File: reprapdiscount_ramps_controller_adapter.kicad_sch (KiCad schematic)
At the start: 5 parts

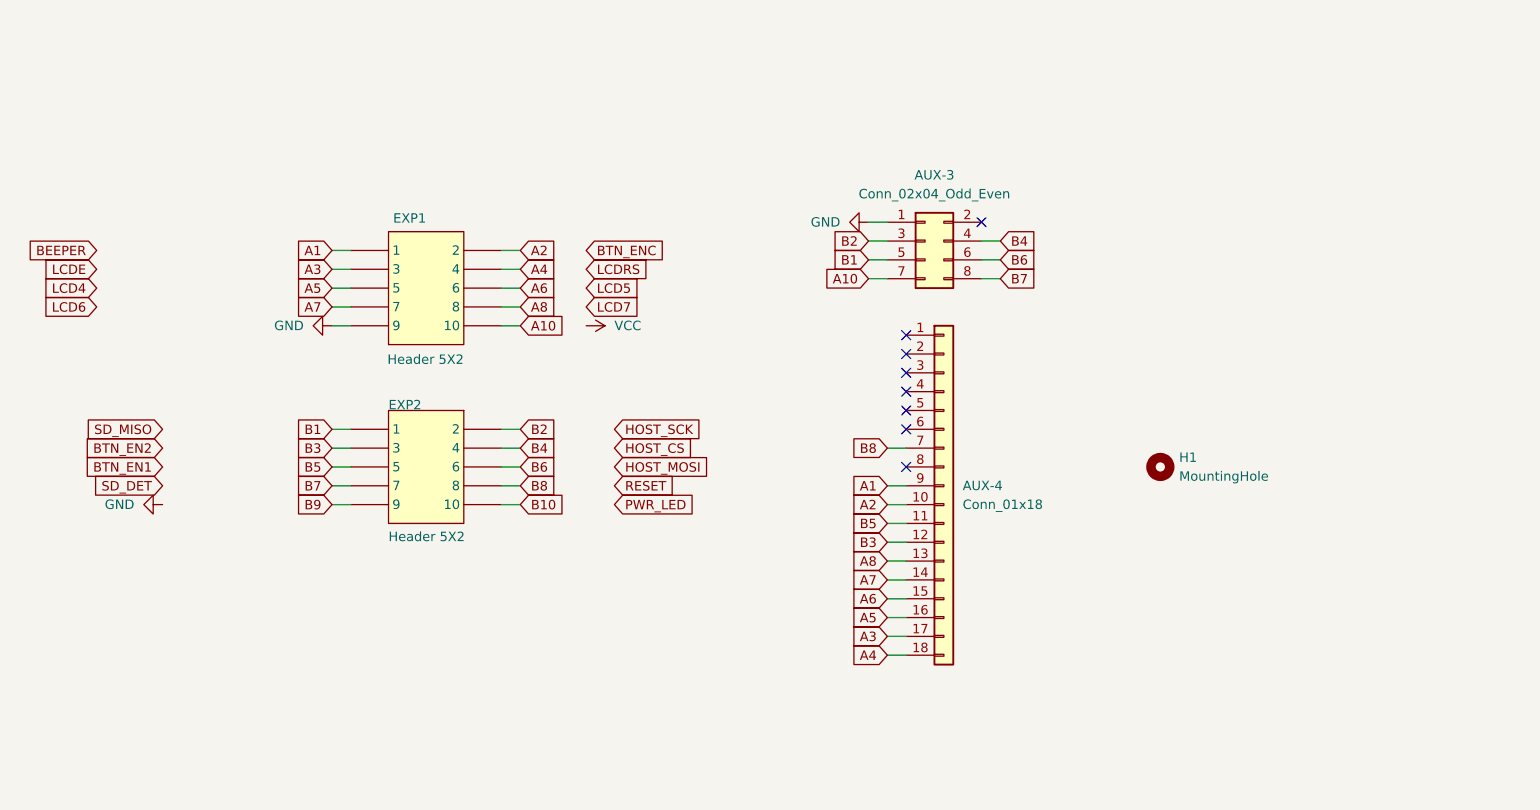
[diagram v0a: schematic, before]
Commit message: adapter: clean up schematic
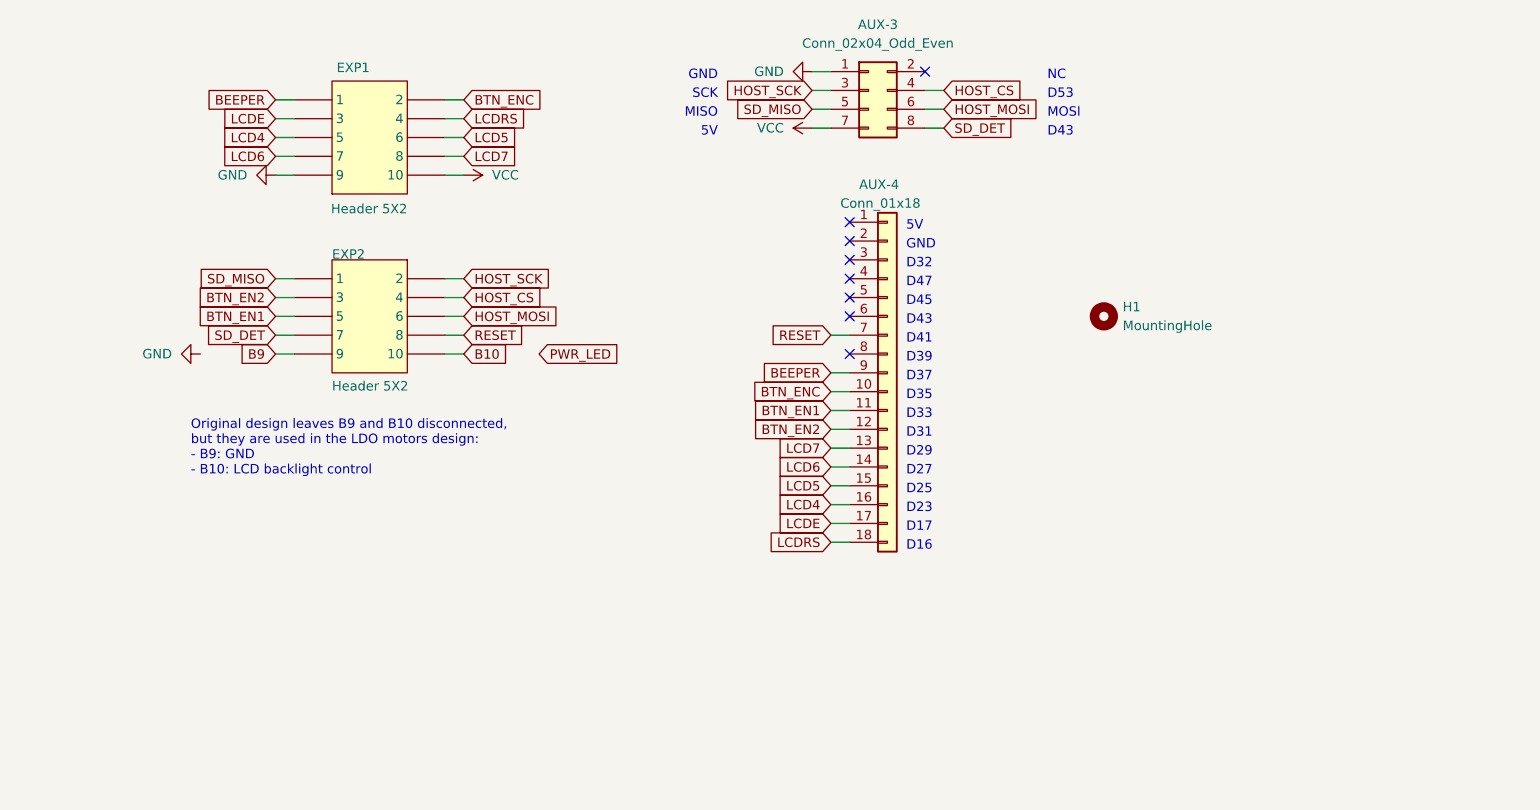
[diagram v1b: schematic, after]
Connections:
- net A1 is gone; now on net BEEPER: AUX-4.9 (Pin_9), EXP1.1
- net A10 is gone; now on net VCC: AUX-3.7 (Pin_7), EXP1.10
- net A2 is gone; now on net BTN_ENC: AUX-4.10 (Pin_10), EXP1.2
- net A3 is gone; now on net LCDE: AUX-4.17 (Pin_17), EXP1.3
- net A4 is gone; now on net LCDRS: AUX-4.18 (Pin_18), EXP1.4
- net A5 is gone; now on net LCD4: AUX-4.16 (Pin_16), EXP1.5
- net A6 is gone; now on net LCD5: AUX-4.15 (Pin_15), EXP1.6
- net A7 is gone; now on net LCD6: AUX-4.14 (Pin_14), EXP1.7
- net A8 is gone; now on net LCD7: AUX-4.13 (Pin_13), EXP1.8
- net B1 is gone; now on net SD_MISO: AUX-3.5 (Pin_5), EXP2.1
- net B2 is gone; now on net HOST_SCK: AUX-3.3 (Pin_3), EXP2.2
- net B3 is gone; now on net BTN_EN2: AUX-4.12 (Pin_12), EXP2.3
- net B4 is gone; now on net HOST_CS: AUX-3.4 (Pin_4), EXP2.4
- net B5 is gone; now on net BTN_EN1: AUX-4.11 (Pin_11), EXP2.5
- net B6 is gone; now on net HOST_MOSI: AUX-3.6 (Pin_6), EXP2.6
- net B7 is gone; now on net SD_DET: AUX-3.8 (Pin_8), EXP2.7
- net B8 is gone; now on net RESET: AUX-4.7 (Pin_7), EXP2.8
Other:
- note added: "5V"
- note added: "D16"
- note added: "D17"
- note added: "D23"
- note added: "D25"
- note added: "D27"
- note added: "D29"
- note added: "D31"
- note added: "D32"
- note added: "D33"
- note added: "D35"
- note added: "D37"
- note added: "D39"
- note added: "D41"
- note added: "D43"
- note added: "D45"
- note added: "D47"
- note added: "D53"
- note added: "GND"
- note added: "MISO"
- note added: "MOSI"
- note added: "NC"
- note added: "Original design leaves B9 and B10 disconnected, but they are used in the LDO motors design: - B9: GND - B10: LCD backlight control"
- note added: "SCK"
- moved on the sheet: AUX-3, AUX-4, EXP1, EXP2, H1

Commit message: adapter: setup ci
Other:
- title: (none) -> RepRapDiscount.com Ramps Smart Adapter
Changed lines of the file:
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@@
 (kicad_sch (version 20230121) (generator eeschema)
   (paper "A4")
+  (title_block
+    (title "RepRapDiscount.com Ramps Smart Adapter")
+    (date "${DATE}")
+    (rev "${TAG} (${HASH})")
+  )
   (no_connect (at 180.34 59.69))
   (no_connect (at 170.18 92.71))

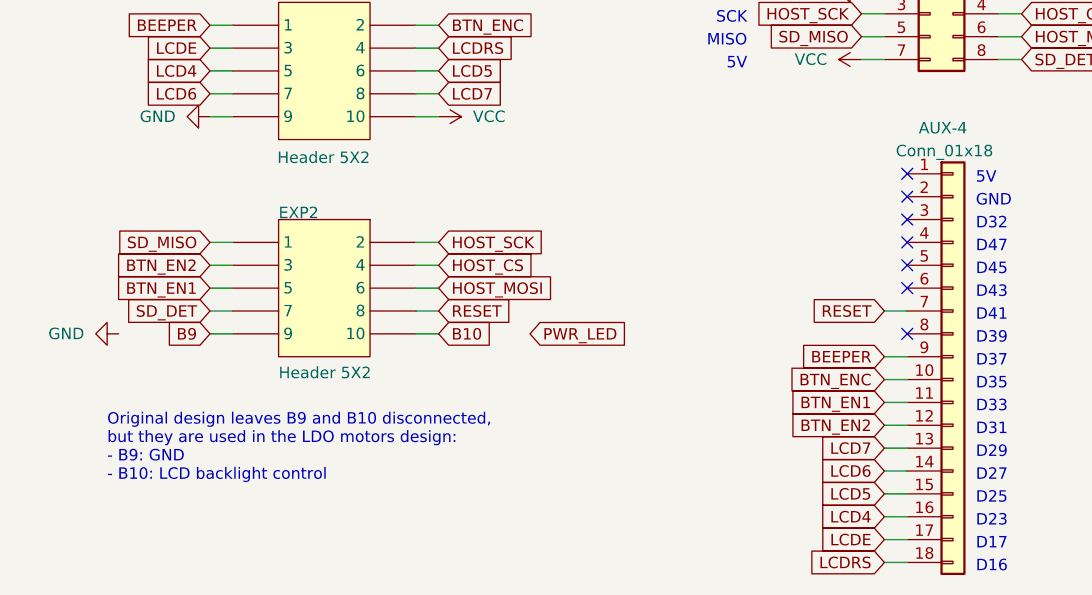
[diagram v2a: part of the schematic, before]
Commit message: adapter: add ldo connections
- adapter: update silkscreen
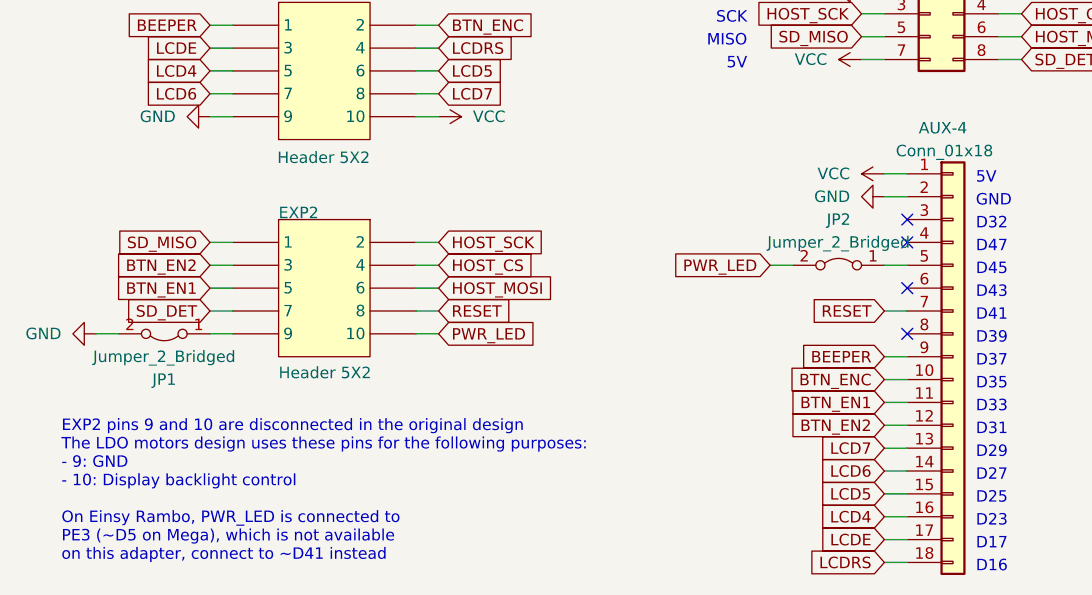
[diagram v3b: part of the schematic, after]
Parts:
- added JP1, JP2: Jumper_2_Bridged, Jumper:SolderJumper-2_P1.3mm_Bridged_RoundedPad1.0x1.5mm, symbol Jumper:Jumper_2_Bridged
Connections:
- net B10 is gone; now on net PWR_LED: EXP2.10
- net GND: now also AUX-4.2 (Pin_2), JP1.2 (B)
- net PWR_LED: now also JP2.2 (B)
- net VCC: now also AUX-4.1 (Pin_1)
- net at AUX-4.5 (Pin_5): now also JP2.1 (A)
- net B9: no longer names the net of EXP2.9
- net B9: now also JP1.1 (A)
- no-connect marks 8 -> 5
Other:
- note added: "EXP2 pins 9 and 10 are disconnected in the original design The LDO motors design uses these pins for the following purposes: - 9: GND - 10: Display backlight control On Einsy Rambo, PWR_LED is connected to PE3 (~D5 on Mega), which is not available on this adapter, connect to ~D41 instead"
- note removed: "Original design leaves B9 and B10 disconnected, but they are used in the LDO motors design: - B9: GND - B10: LCD backlight control"
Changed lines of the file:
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@@
   (no_connect (at 170.18 97.79))
   (no_connect (at 170.18 85.09))
-  (no_connect (at 170.18 90.17))
-  (no_connect (at 170.18 82.55))
-  (no_connect (at 170.18 80.01))
   (no_connect (at 170.18 87.63))
   (wire (pts (xy 92.71 95.25) (xy 95.25 95.25))
     (stroke (width 0) (type default))
   )
+  (wire (pts (xy 167.64 82.55) (xy 170.18 82.55))
+    (stroke (width 0) (type default))
+  )
   (wire (pts (xy 115.57 95.25) (xy 118.11 95.25))
     (stroke (width 0) (type default))
@@
     (stroke (width 0) (type default))
   )
+  (wire (pts (xy 167.64 80.01) (xy 170.18 80.01))
+    (stroke (width 0) (type default))
+  )
   (wire (pts (xy 167.64 95.25) (xy 170.18 95.25))
     (stroke (width 0) (type default))
@@
     (stroke (width 0) (type default))
   )
+  (wire (pts (xy 80.01 97.79) (xy 82.55 97.79))
+    (stroke (width 0) (type default))
+  )
   (wire (pts (xy 165.1 67.31) (xy 167.64 67.31))
     (stroke (width 0) (type default))
@@
     (stroke (width 0) (type default))
   )
+  (wire (pts (xy 154.94 90.17) (xy 157.48 90.17))
+    (stroke (width 0) (type default))
+  )
   (wire (pts (xy 95.25 71.12) (xy 92.71 71.12))
     (stroke (width 0) (type default))
@@
   )
   (wire (pts (xy 167.64 107.95) (xy 170.18 107.95))
+    (stroke (width 0) (type default))
+  )
+  (wire (pts (xy 167.64 90.17) (xy 170.18 90.17))
     (stroke (width 0) (type default))
   )
@@
     (effects (font (size 1.27 1.27)) (justify left bottom))
   )
+  (text "EXP2 pins 9 and 10 are disconnected in the original design\nThe LDO motors design uses these pins for the following purposes:\n- 9: GND\n- 10: Display backlight control\n\nOn Einsy Rambo, PWR_LED is connected to \nPE3 (~D5 on Mega), which is not available \non this adapter, connect to ~D41 instead"
+    (at 76.2 123.19 0)
+    (effects (font (size 1.27 1.27)) (justify left bottom))
+  )
   (text "D32" (at 177.8 86.36 0)
     (effects (font (size 1.27 1.27)) (justify left bottom))
@@
     (effects (font (size 1.27 1.27)) (justify left bottom))
   )
-  (text "Original design leaves B9 and B10 disconnected, \nbut they are used in the LDO motors design:\n- B9: GND\n- B10: LCD backlight control"
-    (at 81.28 114.3 0)
-    (effects (font (size 1.27 1.27)) (justify left bottom))
-  )
   (text "D53" (at 196.85 63.5 0)
     (effects (font (size 1.27 1.27)) (justify left bottom))
@@
     )
   )
+  (global_label "PWR_LED" (shape input) (at 154.94 90.17 180) (fields_autoplaced)
+    (effects (font (size 1.27 1.27)) (justify right))
+    (property "Intersheetrefs" "${INTERSHEET_REFS}" (at 143.6281 90.17 0)
+      (effects (font (size 1.27 1.27)) (justify right) hide)
+    )
+  )
   (global_label "HOST_SCK" (shape input) (at 118.11 87.63 0) (fields_autoplaced)
     (effects (font (size 1.27 1.27)) (justify left))
@@
     )
   )
-  (global_label "PWR_LED" (shape input) (at 128.27 97.79 0) (fields_autoplaced)
-    (effects (font (size 1.27 1.27)) (justify left))
-    (property "Intersheetrefs" "${INTERSHEET_REFS}" (at 139.5819 97.79 0)
+  (global_label "PWR_LED" (shape input) (at 118.11 97.79 0) (fields_autoplaced)
+    (effects (font (size 1.27 1.27)) (justify left))
+    (property "Intersheetrefs" "${INTERSHEET_REFS}" (at 129.4219 97.79 0)
       (effects (font (size 1.27 1.27)) (justify left) hide)
     )
@@
     )
   )
-  (global_label "B10" (shape input) (at 118.11 97.79 0) (fields_autoplaced)
-    (effects (font (size 1.27 1.27)) (justify left))
-    (property "Intersheetrefs" "${INTERSHEET_REFS}" (at 124.7048 97.79 0)
-      (effects (font (size 1.27 1.27)) (justify left) hide)
-    )
-  )
-  (global_label "B9" (shape input) (at 92.71 97.79 180) (fields_autoplaced)
-    (effects (font (size 1.27 1.27)) (justify right))
-    (property "Intersheetrefs" "${INTERSHEET_REFS}" (at 87.3247 97.79 0)
-      (effects (font (size 1.27 1.27)) (justify right) hide)
-    )
-  )
   (global_label "LCD6" (shape input) (at 92.71 71.12 180) (fields_autoplaced)
     (effects (font (size 1.27 1.27)) (justify right))
@@
     )
   )
-  (symbol (lib_id "power:GND") (at 82.55 97.79 270) (unit 1)
-    (in_bom yes) (on_board yes) (dnp no) (fields_autoplaced)
-    (property "Reference" "#PWR03" (at 76.2 97.79 0)
-      (effects (font (size 1.27 1.27)) hide)
-    )
-    (property "Value" "GND" (at 78.74 97.79 90)
+  (symbol (lib_id "power:GND") (at 80.01 97.79 270) (unit 1)
+    (in_bom yes) (on_board yes) (dnp no)
+    (property "Reference" "#PWR03" (at 73.66 97.79 0)
+      (effects (font (size 1.27 1.27)) hide)
+    )
+    (property "Value" "GND" (at 76.2 97.79 90)
       (effects (font (size 1.27 1.27)) (justify right))
     )
-    (property "Footprint" "" (at 82.55 97.79 0)
-      (effects (font (size 1.27 1.27)) hide)
-    )
-    (property "Datasheet" "" (at 82.55 97.79 0)
+    (property "Footprint" "" (at 80.01 97.79 0)
+      (effects (font (size 1.27 1.27)) hide)
+    )
+    (property "Datasheet" "" (at 80.01 97.79 0)
       (effects (font (size 1.27 1.27)) hide)
     )
@@
         (path "/c20eb3f6-d157-43e2-84ab-82664a430dd1/be849d88-3024-45d5-8ff2-8e62174be24e"
           (reference "#PWR04") (unit 1)
+        )
+      )
+    )
+  )
+  (symbol (lib_id "Jumper:Jumper_2_Bridged") (at 87.63 97.79 180) (unit 1)
+    (in_bom yes) (on_board yes) (dnp no)
+    (property "Reference" "JP1" (at 87.63 102.87 0)
+      (effects (font (size 1.27 1.27)))
+    )
+    (property "Value" "Jumper_2_Bridged" (at 87.63 100.33 0)
+      (effects (font (size 1.27 1.27)))
+    )
+    (property "Footprint" "Jumper:SolderJumper-2_P1.3mm_Bridged_RoundedPad1.0x1.5mm" (at 87.63 97.79 0)
+      (effects (font (size 1.27 1.27)) hide)
+    )
+    (property "Datasheet" "~" (at 87.63 97.79 0)
+      (effects (font (size 1.27 1.27)) hide)
+    )
+    (pin "1")
+    (pin "2")
+    (instances
+      (project "reprapdiscount_ramps_controller_adapter"
+        (path "/90758f10-1d2e-4059-a9a5-3e94bccaf518"
+          (reference "JP1") (unit 1)
         )
       )
@@
     )
   )
+  (symbol (lib_id "Jumper:Jumper_2_Bridged") (at 162.56 90.17 0) (mirror y) (unit 1)
+    (in_bom yes) (on_board yes) (dnp no)
+    (property "Reference" "JP2" (at 162.56 85.09 0)
+      (effects (font (size 1.27 1.27)))
+    )
+    (property "Value" "Jumper_2_Bridged" (at 162.56 87.63 0)
+      (effects (font (size 1.27 1.27)))
+    )
+    (property "Footprint" "Jumper:SolderJumper-2_P1.3mm_Bridged_RoundedPad1.0x1.5mm" (at 162.56 90.17 0)
+      (effects (font (size 1.27 1.27)) hide)
+    )
+    (property "Datasheet" "~" (at 162.56 90.17 0)
+      (effects (font (size 1.27 1.27)) hide)
+    )
+    (pin "1")
+    (pin "2")
+    (instances
+      (project "reprapdiscount_ramps_controller_adapter"
+        (path "/90758f10-1d2e-4059-a9a5-3e94bccaf518"
+          (reference "JP2") (unit 1)
+        )
+      )
+    )
+  )
   (symbol (lib_id "power:VCC") (at 118.11 73.66 270) (unit 1)
     (in_bom yes) (on_board yes) (dnp no) (fields_autoplaced)
@@
     )
   )
+  (symbol (lib_id "power:VCC") (at 167.64 80.01 90) (unit 1)
+    (in_bom yes) (on_board yes) (dnp no) (fields_autoplaced)
+    (property "Reference" "#PWR06" (at 171.45 80.01 0)
+      (effects (font (size 1.27 1.27)) hide)
+    )
+    (property "Value" "VCC" (at 163.83 80.01 90)
+      (effects (font (size 1.27 1.27)) (justify left))
+    )
+    (property "Footprint" "" (at 167.64 80.01 0)
+      (effects (font (size 1.27 1.27)) hide)
+    )
+    (property "Datasheet" "" (at 167.64 80.01 0)
+      (effects (font (size 1.27 1.27)) hide)
+    )
+    (pin "1")
+    (instances
+      (project "reprapdiscount_ramps_controller_adapter"
+        (path "/90758f10-1d2e-4059-a9a5-3e94bccaf518"
+          (reference "#PWR06") (unit 1)
+        )
+      )
+      (project "reprapdiscount_smart_controller"
+        (path "/c20eb3f6-d157-43e2-84ab-82664a430dd1"
+          (reference "#PWR014") (unit 1)
+        )
+        (path "/c20eb3f6-d157-43e2-84ab-82664a430dd1/be849d88-3024-45d5-8ff2-8e62174be24e"
+          (reference "#PWR04") (unit 1)
+        )
+      )
+    )
+  )
   (symbol (lib_id "power:GND") (at 165.1 59.69 270) (unit 1)
     (in_bom yes) (on_board yes) (dnp no) (fields_autoplaced)
@@
         )
       )
+      (project "reprapdiscount_smart_controller"
+        (path "/c20eb3f6-d157-43e2-84ab-82664a430dd1"
+          (reference "#PWR016") (unit 1)
+        )
+        (path "/c20eb3f6-d157-43e2-84ab-82664a430dd1/be849d88-3024-45d5-8ff2-8e62174be24e"
+          (reference "#PWR014") (unit 1)
+        )
+      )
+    )
+  )
+  (symbol (lib_id "power:GND") (at 167.64 82.55 270) (unit 1)
+    (in_bom yes) (on_board yes) (dnp no) (fields_autoplaced)
+    (property "Reference" "#PWR07" (at 161.29 82.55 0)
+      (effects (font (size 1.27 1.27)) hide)
+    )
+    (property "Value" "GND" (at 163.83 82.55 90)
+      (effects (font (size 1.27 1.27)) (justify right))
+    )
+    (property "Footprint" "" (at 167.64 82.55 0)
+      (effects (font (size 1.27 1.27)) hide)
+    )
+    (property "Datasheet" "" (at 167.64 82.55 0)
+      (effects (font (size 1.27 1.27)) hide)
+    )
+    (pin "1")
+    (instances
+      (project "reprapdiscount_ramps_controller_adapter"
+        (path "/90758f10-1d2e-4059-a9a5-3e94bccaf518"
+          (reference "#PWR07") (unit 1)
+        )
+      )

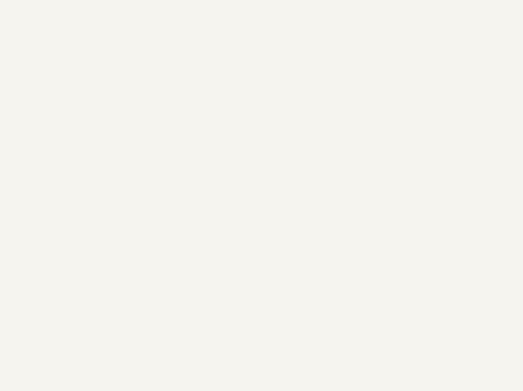
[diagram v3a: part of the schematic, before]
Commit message: all: add oshw logo to design
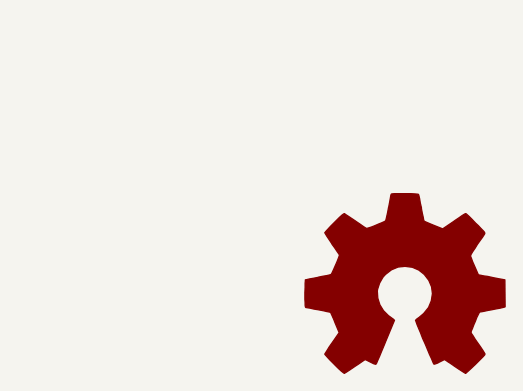
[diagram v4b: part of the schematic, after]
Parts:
- added SYM1: Logo_Open_Hardware_Large, Gigahawk:OSHW-Logo2_7.3x6mm_Mask, symbol Graphic:Logo_Open_Hardware_Large
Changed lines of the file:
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@@
+    )
+  )
+  (symbol (lib_id "Graphic:Logo_Open_Hardware_Large") (at 250.19 148.59 0) (unit 1)
+    (in_bom no) (on_board yes) (dnp no) (fields_autoplaced)
+    (property "Reference" "SYM1" (at 250.19 135.89 0)
+      (effects (font (size 1.27 1.27)) hide)
+    )
+    (property "Value" "Logo_Open_Hardware_Large" (at 250.19 158.75 0)
+      (effects (font (size 1.27 1.27)) hide)
+    )
+    (property "Footprint" "Gigahawk:OSHW-Logo2_7.3x6mm_Mask" (at 250.19 148.59 0)
+      (effects (font (size 1.27 1.27)) hide)
+    )
+    (property "Datasheet" "~" (at 250.19 148.59 0)
+      (effects (font (size 1.27 1.27)) hide)
+    )
+    (property "Sim.Enable" "0" (at 250.19 148.59 0)
+      (effects (font (size 1.27 1.27)) hide)
+    )
+    (instances
+      (project "reprapdiscount_ramps_controller_adapter"
+        (path "/90758f10-1d2e-4059-a9a5-3e94bccaf518"
+          (reference "SYM1") (unit 1)
+        )
+      )
     )
   )
